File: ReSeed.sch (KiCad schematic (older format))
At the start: 45 parts, among them CN1 EDGE_CONNECTOR, CN2 AUDIO_OUT, CN3 AUDIO_IN, CN4 DB9_MALE, Q1 2SC1815, SW1 SW_DIGIFIX, U1 MOS_8580, U2 CD4520BE, U3 74LS245, U4 GAL16V8, U5 TL497ACN

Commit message: Feuer und Wasser
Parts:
- added C17: 100n, Capacitor_THT:C_Disc_D7.0mm_W2.5mm_P5.00mm, symbol Device:C
- renumbered C17 to C18, C18 to C19, C6 to C2, C7 to C3, C8 to C4, C2 to C5, C3 to C6, C5 to C7, C4 to C8, R4 to R1, R11 to R10, R5 to R2, R2 to R3, R1 to R4, R3 to R5, R7 to R6, R8 to R7, R9 to R8, R10 to R9
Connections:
- net +9V: now also C17.1
- net GND: now also C17.2
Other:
- moved on the sheet: R10, R9
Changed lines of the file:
@@
 Sheet 1 1
 Title "ReSeed"
-Date "2022-02-16"
+Date "2022-02-20"
 Rev "1git"
 Comp "SukkoPera/Kinmami"
@@
 	6930 9415 6930 9315
 $Comp
-L Device:R R9
+L Device:R R8
 U 1 1 62099265
 P 6930 9165
-F 0 "R9" H 7000 9211 50  0000 L CNN
+F 0 "R8" H 7000 9211 50  0000 L CNN
 F 1 "1 1%/0.5W" H 7000 9120 50  0000 L CNN
 F 2 "Resistor_THT:R_Axial_DIN0207_L6.3mm_D2.5mm_P10.16mm_Horizontal" V 6860 9165 50  0001 C CNN
@@
 Connection ~ 8860 9215
 $Comp
+L Device:R R9
+U 1 1 620A6D4F
+P 10020 9815
+F 0 "R9" V 9813 9815 50  0000 C CNN
+F 1 "7.87k 1%" V 9904 9815 50  0000 C CNN
+F 2 "Resistor_THT:R_Axial_DIN0207_L6.3mm_D2.5mm_P10.16mm_Horizontal" V 9950 9815 50  0001 C CNN
+F 3 "~" H 10020 9815 50  0001 C CNN
+F 4 "71-CMF557K8700FHEK" H 10020 9815 50  0001 C CNN "MouserPN"
+	1    10020 9815
+	0    1    1    0
+$EndComp
+$Comp
 L Device:R R10
-U 1 1 620A6D4F
-P 9480 9815
-F 0 "R10" V 9273 9815 50  0000 C CNN
-F 1 "7.87k 1%" V 9364 9815 50  0000 C CNN
-F 2 "Resistor_THT:R_Axial_DIN0207_L6.3mm_D2.5mm_P10.16mm_Horizontal" V 9410 9815 50  0001 C CNN
-F 3 "~" H 9480 9815 50  0001 C CNN
-F 4 "71-CMF557K8700FHEK" H 9480 9815 50  0001 C CNN "MouserPN"
-	1    9480 9815
-	0    1    1    0
-$EndComp
-$Comp
-L Device:R R11
 U 1 1 620A853F
-P 9730 10065
-F 0 "R11" H 9660 10019 50  0000 R CNN
-F 1 "1.2k 1%" H 9660 10110 50  0000 R CNN
-F 2 "Resistor_THT:R_Axial_DIN0207_L6.3mm_D2.5mm_P10.16mm_Horizontal" V 9660 10065 50  0001 C CNN
-F 3 "~" H 9730 10065 50  0001 C CNN
-F 4 "603-MF0207FTE52-1K2" H 9730 10065 50  0001 C CNN "MouserPN"
-	1    9730 10065
+P 10270 10065
+F 0 "R10" H 10200 10019 50  0000 R CNN
+F 1 "1.2k 1%" H 10200 10110 50  0000 R CNN
+F 2 "Resistor_THT:R_Axial_DIN0207_L6.3mm_D2.5mm_P10.16mm_Horizontal" V 10200 10065 50  0001 C CNN
+F 3 "~" H 10270 10065 50  0001 C CNN
+F 4 "603-MF0207FTE52-1K2" H 10270 10065 50  0001 C CNN "MouserPN"
+	1    10270 10065
 	-1   0    0    1
 $EndComp
 Wire Wire Line
-	9630 9815 9730 9815
-Wire Wire Line
-	9730 9815 9730 9915
-Wire Wire Line
-	9730 9815 9730 8915
-Wire Wire Line
-	9730 8915 7635 8915
+	10170 9815 10270 9815
+Wire Wire Line
+	10270 9815 10270 9915
+Wire Wire Line
+	10270 9815 10270 8915
+Wire Wire Line
+	10270 8915 7635 8915
 Wire Wire Line
 	7635 8915 7635 9315
 Wire Wire Line
 	7635 9315 7720 9315
-Connection ~ 9730 9815
+Connection ~ 10270 9815
 $Comp
 L Device:CP1 C16
@@
 Connection ~ 9015 9815
 Wire Wire Line
-	9015 9815 9330 9815
+	9015 9815 9715 9815
 Wire Wire Line
 	9015 10295 9015 10405
 Wire Wire Line
-	9015 10405 9730 10405
-Wire Wire Line
-	9730 10405 9730 10215
+	9015 10405 9715 10405
+Wire Wire Line
+	10270 10405 10270 10215
 Wire Wire Line
 	8860 10405 9015 10405
@@
 $EndComp
 $Comp
-L Device:C C6
+L Device:C C2
 U 1 1 620D3E15
 P 6510 1825
-F 0 "C6" H 6395 1871 50  0000 R CNN
+F 0 "C2" H 6395 1871 50  0000 R CNN
 F 1 "22n" H 6395 1780 50  0000 R CNN
 F 2 "Capacitor_THT:C_Disc_D7.0mm_W2.5mm_P5.00mm" H 6548 1675 50  0001 C CNN
@@
 	9505 1720 9565 1720
 $Comp
-L Device:R R5
+L Device:R R2
 U 1 1 6224D360
 P 9715 1720
-F 0 "R5" V 9670 1560 50  0000 C CNN
+F 0 "R2" V 9670 1560 50  0000 C CNN
 F 1 "100" V 9810 1720 50  0000 C CNN
 F 2 "Resistor_THT:R_Axial_DIN0207_L6.3mm_D2.5mm_P10.16mm_Horizontal" V 9645 1720 50  0001 C CNN
@@
 	9505 1920 9505 1720
 $Comp
-L Device:R R4
+L Device:R R1
 U 1 1 6224C319
 P 9715 1620
-F 0 "R4" V 9660 1465 50  0000 C CNN
+F 0 "R1" V 9660 1465 50  0000 C CNN
 F 1 "100" V 9620 1620 50  0000 C CNN
 F 2 "Resistor_THT:R_Axial_DIN0207_L6.3mm_D2.5mm_P10.16mm_Horizontal" V 9645 1620 50  0001 C CNN
@@
 	9230 1320 10705 1320
 $Comp
-L Device:C C7
+L Device:C C3
 U 1 1 622A92D6
 P 8950 2985
-F 0 "C7" H 8695 3030 50  0000 L CNN
+F 0 "C3" H 8695 3030 50  0000 L CNN
 F 1 "3.9n" H 8605 2940 50  0000 L CNN
 F 2 "Capacitor_THT:C_Disc_D7.0mm_W2.5mm_P5.00mm" H 8988 2835 50  0001 C CNN
@@
 $EndComp
 $Comp
-L Device:C C8
+L Device:C C4
 U 1 1 622AA502
 P 9230 2985
-F 0 "C8" H 9345 3031 50  0000 L CNN
+F 0 "C4" H 9345 3031 50  0000 L CNN
 F 1 "3.9n" H 9345 2940 50  0000 L CNN
 F 2 "Capacitor_THT:C_Disc_D7.0mm_W2.5mm_P5.00mm" H 9268 2835 50  0001 C CNN
@@
 ~sid
 $Comp
-L Device:R R1
+L Device:R R4
 U 1 1 63010374
 P 11130 1320
-F 0 "R1" V 10923 1320 50  0000 C CNN
+F 0 "R4" V 10923 1320 50  0000 C CNN
 F 1 "10k" V 11014 1320 50  0000 C CNN
 F 2 "Resistor_THT:R_Axial_DIN0207_L6.3mm_D2.5mm_P10.16mm_Horizontal" V 11060 1320 50  0001 C CNN
@@
 $EndComp
 $Comp
-L Device:C C2
+L Device:C C5
 U 1 1 630231DC
 P 11525 1570
-F 0 "C2" H 11640 1616 50  0000 L CNN
+F 0 "C5" H 11640 1616 50  0000 L CNN
 F 1 "1n" H 11640 1525 50  0000 L CNN
 F 2 "Capacitor_THT:C_Disc_D7.0mm_W2.5mm_P5.00mm" H 11563 1420 50  0001 C CNN
@@
 U 1 1 6305E4B6
 P 12440 1320
-F 0 "Q1" H 12631 1366 50  0000 L CNN
-F 1 "2SC1815" H 12631 1275 50  0000 L CNN
+F 0 "Q1" H 12630 1366 50  0000 L CNN
+F 1 "2SC1815" H 12630 1275 50  0000 L CNN
 F 2 "Package_TO_SOT_THT:TO-92_HandSolder" H 12640 1245 50  0001 L CIN
 F 3 "https://www.onsemi.com/pub/Collateral/BC550-D.pdf" H 12440 1320 50  0001 L CNN
@@
 $EndComp
 $Comp
-L Device:C C3
+L Device:C C6
 U 1 1 63071B14
 P 12275 1625
-F 0 "C3" V 12435 1625 50  0000 C CNN
+F 0 "C6" V 12435 1625 50  0000 C CNN
 F 1 "470p" V 12526 1625 50  0000 C CNN
 F 2 "Capacitor_THT:C_Disc_D7.0mm_W2.5mm_P5.00mm" H 12313 1475 50  0001 C CNN
@@
 $EndComp
 $Comp
-L Device:R R3
+L Device:R R5
 U 1 1 630725DE
 P 12540 1905
-F 0 "R3" H 12470 1859 50  0000 R CNN
+F 0 "R5" H 12470 1859 50  0000 R CNN
 F 1 "1k" H 12470 1950 50  0000 R CNN
 F 2 "Resistor_THT:R_Axial_DIN0207_L6.3mm_D2.5mm_P10.16mm_Horizontal" V 12470 1905 50  0001 C CNN
@@
 Wire Wire Line
 	12540 1625 12880 1625
-$Comp
-L Device:CP1 C4
-U 1 1 6310CD9B
-P 13030 1625
-F 0 "C4" V 13282 1625 50  0000 C CNN
-F 1 "10u" V 13191 1625 50  0000 C CNN
-F 2 "Capacitor_THT:CP_Radial_D5.0mm_P2.00mm" H 13030 1625 50  0001 C CNN
-F 3 "~" H 13030 1625 50  0001 C CNN
-F 4 "710-860010472002" H 13030 1625 50  0001 C CNN "MouserPN"
-	1    13030 1625
-	0    -1   -1   0
-$EndComp
 $Comp
 L Device:R_POT RV1
@@
 $EndComp
 $Comp
-L Device:R R8
+L Device:R R7
 U 1 1 633EFCCD
 P 13515 3295
-F 0 "R8" H 13445 3249 50  0000 R CNN
+F 0 "R7" H 13445 3249 50  0000 R CNN
 F 1 "100k" H 13445 3340 50  0000 R CNN
 F 2 "Resistor_THT:R_Axial_DIN0207_L6.3mm_D2.5mm_P10.16mm_Horizontal" V 13445 3295 50  0001 C CNN
@@
 Text Notes 9180 8520 0    50   ~ 0
 THIS CIRCUIT CAN PRODUCE EITHER\n+9V (140mA MAX) OR +12V (100mA MAX)\nBY CHANGING R1 ONLY.  USE +12V FOR\nMOS 6581 AND +9V FOR MOS 8580.
-Text Notes 9640 9535 2    50   ~ 0
+Text Notes 10180 9535 2    50   ~ 0
 USE 11K FOR\nMOS 6581
 $Comp
@@
 $EndComp
 $Comp
-L Device:C C18
+L Device:C C19
 U 1 1 63F74F81
 P 5990 9490
-F 0 "C18" H 6105 9536 50  0000 L CNN
+F 0 "C19" H 6105 9536 50  0000 L CNN
 F 1 "100n" H 6105 9445 50  0000 L CNN
 F 2 "Capacitor_THT:C_Disc_D7.0mm_W2.5mm_P5.00mm" H 6028 9340 50  0001 C CNN
@@
 $EndComp
 $Comp
-L Device:CP1 C17
+L Device:CP1 C18
 U 1 1 63F75867
 P 5260 9490
-F 0 "C17" H 5375 9536 50  0000 L CNN
+F 0 "C18" H 5375 9536 50  0000 L CNN
 F 1 "100u/16V" H 5375 9445 50  0000 L CNN
 F 2 "Capacitor_THT:CP_Radial_D6.3mm_P2.50mm" H 5260 9490 50  0001 C CNN
@@
 Connection ~ 14650 1645
 $Comp
-L Device:R R2
+L Device:R R3
 U 1 1 64257402
 P 10705 1600
-F 0 "R2" H 10635 1554 50  0000 R CNN
+F 0 "R3" H 10635 1554 50  0000 R CNN
 F 1 "1k" H 10635 1645 50  0000 R CNN
 F 2 "Resistor_THT:R_Axial_DIN0207_L6.3mm_D2.5mm_P10.16mm_Horizontal" V 10635 1600 50  0001 C CNN
@@
 	12540 940  12540 815
 $Comp
-L Device:C C5
+L Device:C C7
 U 1 1 642BE109
 P 13030 940
-F 0 "C5" V 13190 940 50  0000 C CNN
+F 0 "C7" V 13190 940 50  0000 C CNN
 F 1 "100n" V 13281 940 50  0000 C CNN
 F 2 "Capacitor_THT:C_Disc_D7.0mm_W2.5mm_P5.00mm" H 13068 790 50  0001 C CNN
@@
 $EndComp
 $Comp
-L Device:R R7
+L Device:R R6
 U 1 1 6340C3F1
 P 11805 3885
-F 0 "R7" H 11735 3839 50  0000 R CNN
+F 0 "R6" H 11735 3839 50  0000 R CNN
 F 1 "180k" H 11735 3930 50  0000 R CNN
 F 2 "Resistor_THT:R_Axial_DIN0207_L6.3mm_D2.5mm_P10.16mm_Horizontal" V 11735 3885 50  0001 C CNN
@@
 	11805 3600 11805 3735
 NoConn ~ 11955 3450
+$Comp
+L Device:C C17
+U 1 1 6215D5D2
+P 9715 10145
+F 0 "C17" H 9830 10191 50  0000 L CNN
+F 1 "100n" H 9830 10100 50  0000 L CNN
+F 2 "Capacitor_THT:C_Disc_D7.0mm_W2.5mm_P5.00mm" H 9753 9995 50  0001 C CNN
+F 3 "~" H 9715 10145 50  0001 C CNN
+F 4 "810-FG28X7R1H104KNT0" H 9715 10145 50  0001 C CNN "MouserPN"
+	1    9715 10145
+	1    0    0    -1
+$EndComp
+Wire Wire Line
+	9715 10295 9715 10405
+Connection ~ 9715 10405
+Wire Wire Line
+	9715 10405 10270 10405
+Wire Wire Line
+	9715 9995 9715 9815
 Wire Bus Line
 	9365 5800 9365 6055
@@
 Wire Bus Line
 	3870 2725 3870 4225
+Connection ~ 9715 9815
+Wire Wire Line
+	9715 9815 9870 9815
+$Comp
+L Device:CP1 C8
+U 1 1 6310CD9B
+P 13030 1625
+F 0 "C8" V 12870 1625 50  0000 C CNN
+F 1 "10u" V 12779 1625 50  0000 C CNN
+F 2 "Capacitor_THT:CP_Radial_D5.0mm_P2.00mm" H 13030 1625 50  0001 C CNN
+F 3 "~" H 13030 1625 50  0001 C CNN
+F 4 "710-860010472002" H 13030 1625 50  0001 C CNN "MouserPN"
+	1    13030 1625
+	0    -1   -1   0
+$EndComp
 $EndSCHEMATC

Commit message: Ready?
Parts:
- added JP1: JMP_GND_LIFT, Jumper:SolderJumper-2_P1.3mm_Bridged_RoundedPad1.0x1.5mm, symbol Device:Jumper_NC_Small
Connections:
- net GND: now also JP1.1; no longer CN3.RN, CN3.TN
- new net: CN3.TN, JP1.2
- no-connect marks 27 -> 28
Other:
- note added: "WITH NO JACK, AUDIO_IN GETS SHORTED\nTO GND IN ORDER TO AVOID NOISE\n(UNLESS JP1 IS OPENED)"
- note removed: "WITH NO JACK, AUDIO_IN GETS SHORTED\nTO GND IN ORDER TO AVOID NOISE"
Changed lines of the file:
@@
 	13515 3015 14520 3015
-Wire Wire Line
-	14650 3315 14650 3115
 Wire Wire Line
 	14650 2915 14765 2915
 Connection ~ 14650 3315
-Wire Wire Line
-	14765 3115 14650 3115
-Connection ~ 14650 3115
-Wire Wire Line
-	14650 3115 14650 2915
 Wire Wire Line
 	14765 3215 14520 3215
@@
 Text Notes 12445 1180 2    50   ~ 0
 BC549C CAN BE USED TOO,\nWITH HIGHER NOISE THOUGH
-Text Notes 14475 2750 0    50   ~ 0
-WITH NO JACK, AUDIO_IN GETS SHORTED\nTO GND IN ORDER TO AVOID NOISE
+Text Notes 14085 4110 0    50   ~ 0
+WITH NO JACK, AUDIO_IN GETS SHORTED\nTO GND IN ORDER TO AVOID NOISE\n(UNLESS JP1 IS OPENED)
 Text Notes 6425 1640 2    50   ~ 0
 USE 470pF\nFOR 6581
@@
 Wire Wire Line
 	9715 9995 9715 9815
-Wire Bus Line
-	9365 5800 9365 6055
-Wire Bus Line
-	7120 2320 7120 2720
-Wire Bus Line
-	9605 1920 9605 2620
-Wire Bus Line
-	14845 5890 14845 6590
-Wire Bus Line
-	1175 3525 1175 4225
-Wire Bus Line
-	7165 5800 7165 6855
-Wire Bus Line
-	3870 2725 3870 4225
 Connection ~ 9715 9815
 Wire Wire Line
@@
 	0    -1   -1   0
 $EndComp
+NoConn ~ 14765 3115
+$Comp
+L Device:Jumper_NC_Small JP1
+U 1 1 623495F8
+P 14550 2915
+F 0 "JP1" H 14550 3127 50  0000 C CNN
+F 1 "JMP_GND_LIFT" H 14550 3036 50  0000 C CNN
+F 2 "Jumper:SolderJumper-2_P1.3mm_Bridged_RoundedPad1.0x1.5mm" H 14550 2915 50  0001 C CNN
+F 3 "~" H 14550 2915 50  0001 C CNN
+	1    14550 2915
+	1    0    0    -1
+$EndComp
+Wire Wire Line
+	14450 2915 14335 2915
+Wire Wire Line
+	14335 2915 14335 3315
+Wire Wire Line
+	14335 3315 14650 3315
+Wire Bus Line
+	9365 5800 9365 6055
+Wire Bus Line
+	7120 2320 7120 2720
+Wire Bus Line
+	9605 1920 9605 2620
+Wire Bus Line
+	14845 5890 14845 6590
+Wire Bus Line
+	1175 3525 1175 4225
+Wire Bus Line
+	7165 5800 7165 6855
+Wire Bus Line
+	3870 2725 3870 4225
 $EndSCHEMATC

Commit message: Add note about R3
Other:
- note added: "MOUNT FOR MOS\n6581 ONLY"
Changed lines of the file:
@@
 Wire Bus Line
 	3870 2725 3870 4225
+Text Notes 10465 2240 0    50   ~ 0
+MOUNT FOR MOS\n6581 ONLY
 $EndSCHEMATC

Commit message: Change headphone connectors
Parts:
- CN2, CN3: footprint Connector_Audio:Jack_3.5mm_Ledino_KB3SPRS_Horizontal -> ReSeed:AudioJack_SJ1-3525N
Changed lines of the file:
@@
 F 0 "CN3" H 14685 3048 50  0000 R CNN
 F 1 "AUDIO_IN" H 14685 3139 50  0000 R CNN
-F 2 "Connector_Audio:Jack_3.5mm_Ledino_KB3SPRS_Horizontal" H 14965 3215 50  0001 C CNN
+F 2 "ReSeed:AudioJack_SJ1-3525N" H 14965 3215 50  0001 C CNN
 F 3 "~" H 14965 3215 50  0001 C CNN
 	1    14965 3215
@@
 F 0 "CN2" H 14685 1678 50  0000 R CNN
 F 1 "AUDIO_OUT" H 14685 1769 50  0000 R CNN
-F 2 "Connector_Audio:Jack_3.5mm_Ledino_KB3SPRS_Horizontal" H 14965 1845 50  0001 C CNN
+F 2 "ReSeed:AudioJack_SJ1-3525N" H 14965 1845 50  0001 C CNN
 F 3 "~" H 14965 1845 50  0001 C CNN
 	1    14965 1845
@@
 Wire Wire Line
 	14335 3315 14650 3315
-Wire Bus Line
-	9365 5800 9365 6055
-Wire Bus Line
-	7120 2320 7120 2720
-Wire Bus Line
-	9605 1920 9605 2620
-Wire Bus Line
-	14845 5890 14845 6590
-Wire Bus Line
-	1175 3525 1175 4225
-Wire Bus Line
-	7165 5800 7165 6855
-Wire Bus Line
-	3870 2725 3870 4225
 Text Notes 10465 2240 0    50   ~ 0
 MOUNT FOR MOS\n6581 ONLY
+Wire Bus Line
+	9365 5800 9365 6055
+Wire Bus Line
+	7120 2320 7120 2720
+Wire Bus Line
+	9605 1920 9605 2620
+Wire Bus Line
+	14845 5890 14845 6590
+Wire Bus Line
+	1175 3525 1175 4225
+Wire Bus Line
+	7165 5800 7165 6855
+Wire Bus Line
+	3870 2725 3870 4225
 $EndSCHEMATC

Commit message: Change pots
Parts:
- RV1, RV2: footprint ReSeed:Potentiometer_Vertical -> ReSeed:Pot_Bourns_3306P
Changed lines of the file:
@@
 F 0 "RV1" H 13350 1951 50  0000 R CNN
 F 1 "10k" H 13350 1860 50  0000 R CNN
-F 2 "ReSeed:Potentiometer_Vertical" H 13420 1905 50  0001 C CNN
+F 2 "ReSeed:Pot_Bourns_3306P" H 13420 1905 50  0001 C CNN
 F 3 "~" H 13420 1905 50  0001 C CNN
 	1    13420 1905
@@
 F 0 "RV2" V 11598 3450 50  0000 C CNN
 F 1 "1M" V 11689 3450 50  0000 C CNN
-F 2 "ReSeed:Potentiometer_Vertical" H 11805 3450 50  0001 C CNN
+F 2 "ReSeed:Pot_Bourns_3306P" H 11805 3450 50  0001 C CNN
 F 3 "~" H 11805 3450 50  0001 C CNN
 	1    11805 3450

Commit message: Fix BJT P/N
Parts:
- Q1: value 2SC1815 -> BC547C
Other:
- note added: "BC548/9 CAN BE USED TOO.\nA NICE AND LESS NOISY ALTERNATIVE\nWOULD BE 2SC1815, BUT BE AWARE\nTHAT IT HAS A DIFFERENT PINOUT!"
- note removed: "BC549C CAN BE USED TOO,\nWITH HIGHER NOISE THOUGH"
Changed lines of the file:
@@
 Sheet 1 1
 Title "ReSeed"
-Date "2022-02-20"
+Date "2022-10-24"
 Rev "1git"
 Comp "SukkoPera/Kinmami"
@@
 U 1 1 63010374
 P 11130 1320
-F 0 "R4" V 10923 1320 50  0000 C CNN
-F 1 "10k" V 11014 1320 50  0000 C CNN
+F 0 "R4" V 11245 1320 50  0000 C CNN
+F 1 "10k" V 11336 1320 50  0000 C CNN
 F 2 "Resistor_THT:R_Axial_DIN0207_L6.3mm_D2.5mm_P10.16mm_Horizontal" V 11060 1320 50  0001 C CNN
 F 3 "~" H 11130 1320 50  0001 C CNN
@@
 P 12440 1320
 F 0 "Q1" H 12630 1366 50  0000 L CNN
-F 1 "2SC1815" H 12630 1275 50  0000 L CNN
+F 1 "BC547C" H 12630 1275 50  0000 L CNN
 F 2 "Package_TO_SOT_THT:TO-92_HandSolder" H 12640 1245 50  0001 L CIN
 F 3 "https://www.onsemi.com/pub/Collateral/BC550-D.pdf" H 12440 1320 50  0001 L CNN
@@
 Text Notes 12200 8065 0    50   ~ 0
 WHAT HAPPENS IF YOU WRITE TO THE PORT?\nYOU CAN CREATE SHORT CIRCUITS!\nTODO: CONSIDER ADDING DIODES, CONNECTING\nPIN 1 TO VCC OR SWITCHING TO 74244
-Text Notes 12445 1180 2    50   ~ 0
-BC549C CAN BE USED TOO,\nWITH HIGHER NOISE THOUGH
+Text Notes 12445 1175 2    50   ~ 0
+BC548/9 CAN BE USED TOO.\nA NICE AND LESS NOISY ALTERNATIVE\nWOULD BE 2SC1815, BUT BE AWARE\nTHAT IT HAS A DIFFERENT PINOUT!
 Text Notes 14085 4110 0    50   ~ 0
 WITH NO JACK, AUDIO_IN GETS SHORTED\nTO GND IN ORDER TO AVOID NOISE\n(UNLESS JP1 IS OPENED)

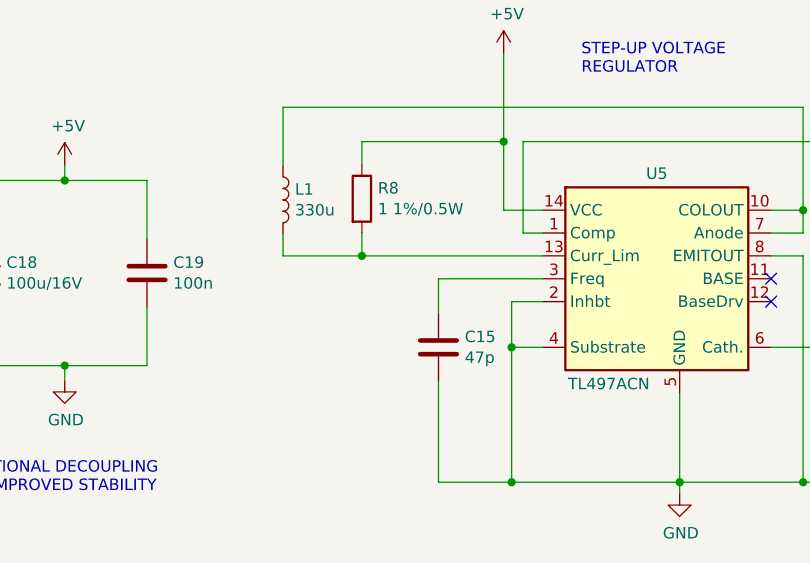
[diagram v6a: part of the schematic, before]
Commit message: Reduce output noise C15 -> 100p, R8 -> 3.3, L1 -> 100u
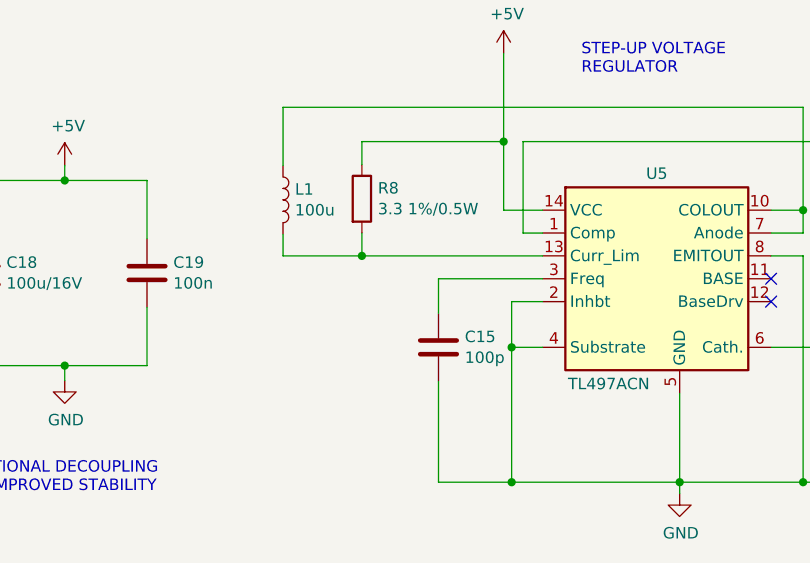
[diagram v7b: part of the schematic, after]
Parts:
- C15: value 47p -> 100p
- L1: value 330u -> 100u
- R8: value 1 1%/0.5W -> 3.3 1%/0.5W
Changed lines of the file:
@@
 Sheet 1 1
 Title "ReSeed"
-Date "2022-10-24"
-Rev "1git"
+Date "2023-01-15"
+Rev "1.1"
 Comp "SukkoPera/Kinmami"
 Comment1 "Replica of Christian Schäffner (Solder)'s SID Card for the Commodore 16/+4"
@@
 P 6930 9165
 F 0 "R8" H 7000 9211 50  0000 L CNN
-F 1 "1 1%/0.5W" H 7000 9120 50  0000 L CNN
+F 1 "3.3 1%/0.5W" H 7000 9120 50  0000 L CNN
 F 2 "Resistor_THT:R_Axial_DIN0207_L6.3mm_D2.5mm_P10.16mm_Horizontal" V 6860 9165 50  0001 C CNN
 F 3 "~" H 6930 9165 50  0001 C CNN
@@
 P 7265 9815
 F 0 "C15" H 7380 9861 50  0000 L CNN
-F 1 "47p" H 7380 9770 50  0000 L CNN
+F 1 "100p" H 7380 9770 50  0000 L CNN
 F 2 "Capacitor_THT:C_Disc_D7.0mm_W2.5mm_P5.00mm" H 7303 9665 50  0001 C CNN
 F 3 "~" H 7265 9815 50  0001 C CNN
@@
 P 6585 9170
 F 0 "L1" H 6637 9216 50  0000 L CNN
-F 1 "330u" H 6637 9125 50  0000 L CNN
+F 1 "100u" H 6637 9125 50  0000 L CNN
 F 2 "Inductor_THT:L_Radial_D8.7mm_P5.00mm_Fastron_07HCP" H 6585 9170 50  0001 C CNN
 F 3 "~" H 6585 9170 50  0001 C CNN
